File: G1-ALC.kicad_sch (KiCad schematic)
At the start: 90 parts, among them J101 Conn_01x03_Pin, J102 330 VAC In, J103 G1 connections, J104 105VAC in, J105 Conn_01x03_Pin, J107 Conn_01x05_Pin, J108 G2 Control board interconnect, Q101 TIP122, U101 LM7812_TO220, U102 LM324, U103 CNY17-4, U301 CNY17-4

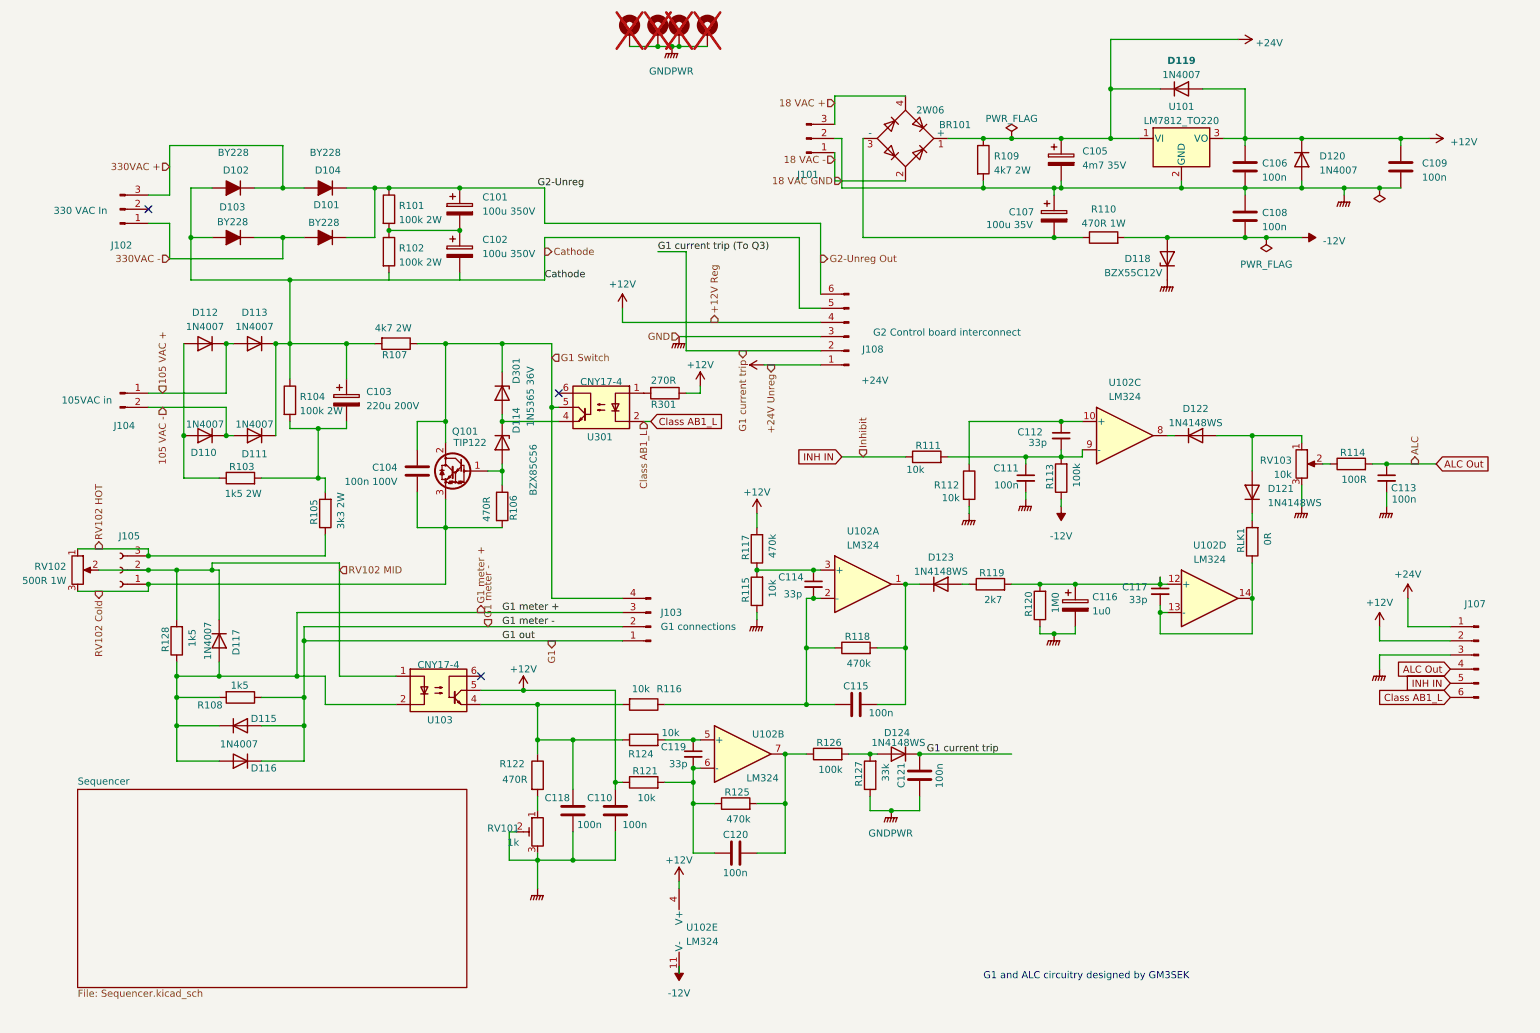
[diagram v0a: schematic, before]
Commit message: Fixes for issuees #1, €2 and #3
Fixed unconnected capacitor and bleeder
Turned connectors around to orient screw connectors with screws outward from the board.
Use new footprint for BY228 diodes with larget pand and holes.

Added a subsheet for notes containing differences with original drawing from GM3SEK.
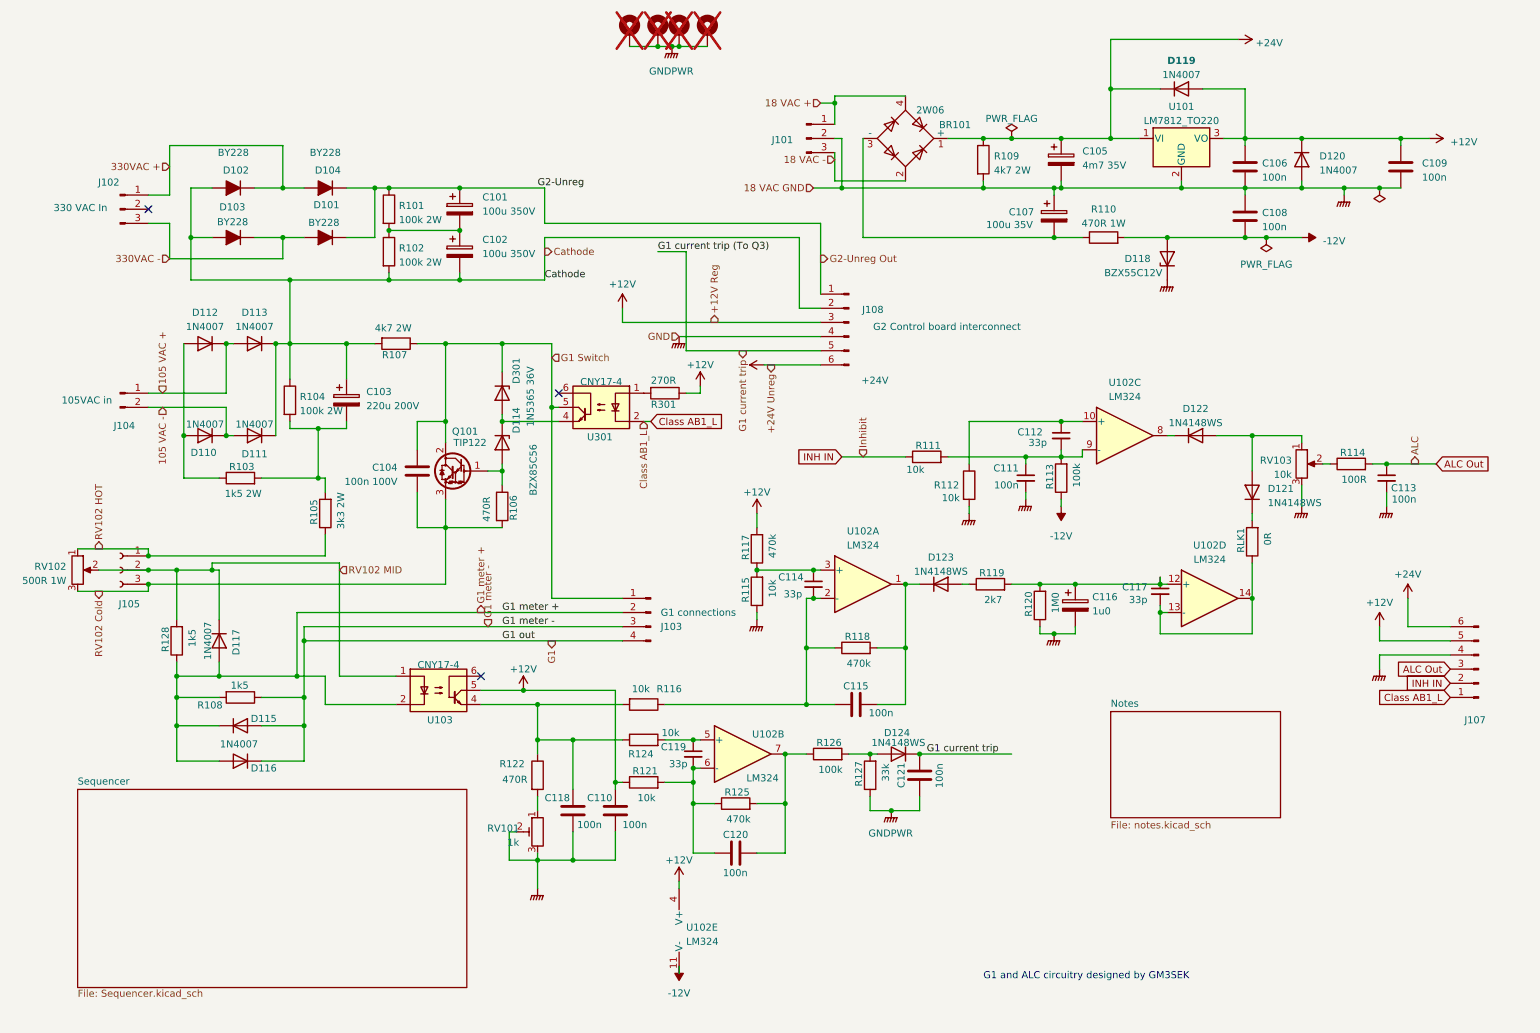
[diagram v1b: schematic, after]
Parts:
- D101, D102, D103, D104: footprint Diode_THT:D_DO-15_P15.24mm_Horizontal -> Diode_THT_AKL:D_SOD-64_P15.24mm_big_holes_Horizontal
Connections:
- net +12V: now also J107.5 (Pin_5), J108.3 (Pin_3); no longer J107.2 (Pin_2), J108.4 (Pin_4)
- net +24V: now also J107.6 (Pin_6), J108.6 (Pin_6); no longer J107.1 (Pin_1), J108.1 (Pin_1)
- net 18 VAC +: now also J101.1 (Pin_1); no longer J101.3 (Pin_3)
- net 330VAC +: now also J102.1 (Pin_1); no longer J102.3 (Pin_3)
- net 330VAC -: now also J102.3 (Pin_3); no longer J102.1 (Pin_1)
- net ALC Out: now also J107.3 (Pin_3); no longer J107.4 (Pin_4)
- net Cathode: now also C102.2, J108.2 (Pin_2), R102.2; no longer J108.5 (Pin_5)
- net Class AB1_L: now also J107.1 (Pin_1); no longer J107.6 (Pin_6)
- net G1: now also J103.3 (Pin_3), J103.4 (Pin_4); no longer J103.1 (Pin_1), J103.2 (Pin_2)
- net G1 Switch: now also J103.1 (Pin_1); no longer J103.4 (Pin_4)
- net G1 current trip: now also J108.5 (Pin_5); no longer J108.2 (Pin_2)
- net G1 meter +: now also J103.2 (Pin_2); no longer J103.3 (Pin_3)
- net G2-Unreg Out: now also J108.1 (Pin_1); no longer J108.6 (Pin_6)
- net GNDPWR: now also J107.4 (Pin_4), J108.4 (Pin_4); no longer BR101.2, J101.1 (Pin_1), J107.3 (Pin_3), J108.3 (Pin_3)
- net INH IN: now also J107.2 (Pin_2); no longer J107.5 (Pin_5)
- net RV102 Cold: now also J105.3 (Pin_3); no longer J105.1 (Pin_1)
- net RV102 HOT: now also J105.1 (Pin_1); no longer J105.3 (Pin_3)
- new net 18 VAC -: BR101.2, J101.3 (Pin_3)
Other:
- added sheet Notes (notes.kicad_sch)
- moved on the sheet: J103, J105, J107, J108

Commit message: Nil
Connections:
- net RV102 Cold: now also J105.1 (Pin_1); no longer J105.3 (Pin_3)
- net RV102 HOT: now also J105.3 (Pin_3); no longer J105.1 (Pin_1)
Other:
- moved on the sheet: J105
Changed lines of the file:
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@@
 	(symbol
 		(lib_id "Connector:Conn_01x03_Socket")
-		(at 33.02 116.84 0)
-		(mirror y)
+		(at 33.02 116.84 180)
 		(unit 1)
 		(exclude_from_sim no)
@@
 		(dnp no)
 		(property "Reference" "J105"
-			(at 34.671 122.936 0)
+			(at 34.671 110.744 0)
 			(effects
 				(font
@@
 		)
 		(property "Value" "Conn_01x03_Pin"
-			(at 33.655 121.412 0)
+			(at 33.655 112.268 0)
 			(effects
 				(font

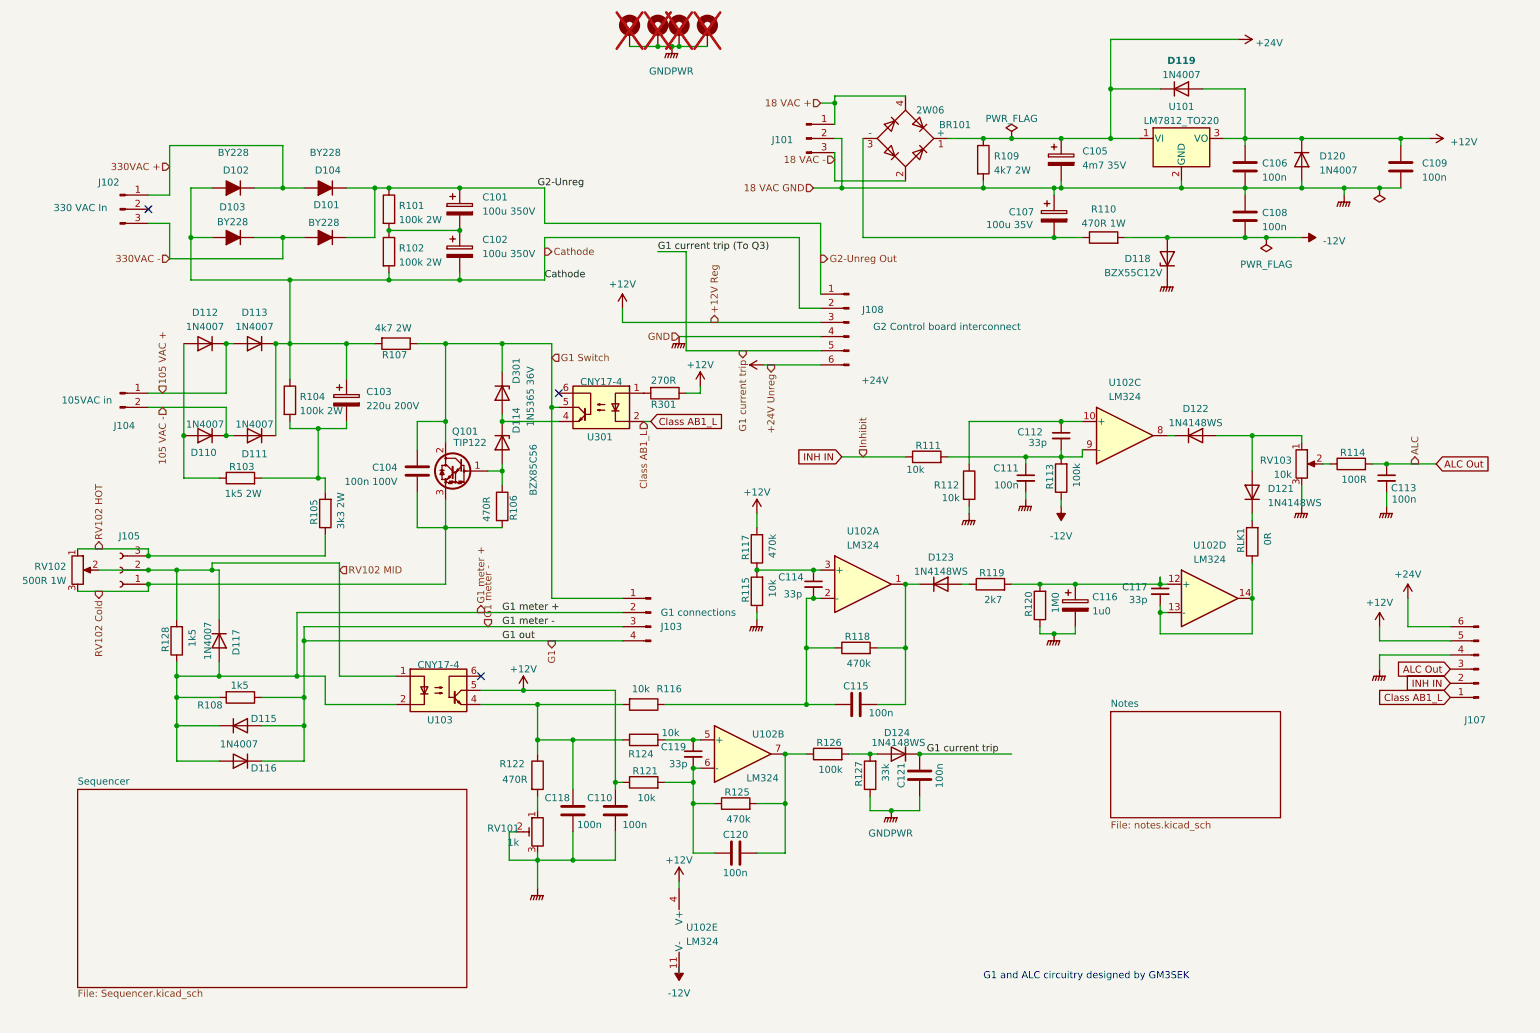
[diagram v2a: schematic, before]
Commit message: Updated junction positions and wire connections in schematic
Performed major modifications to the junction positions and wire connections in the kicad schematic G1-ALC. The changes include removal and addition of certain junction points, repositioning of wires and altering electrical connections to improve schematic efficiency and accuracy.
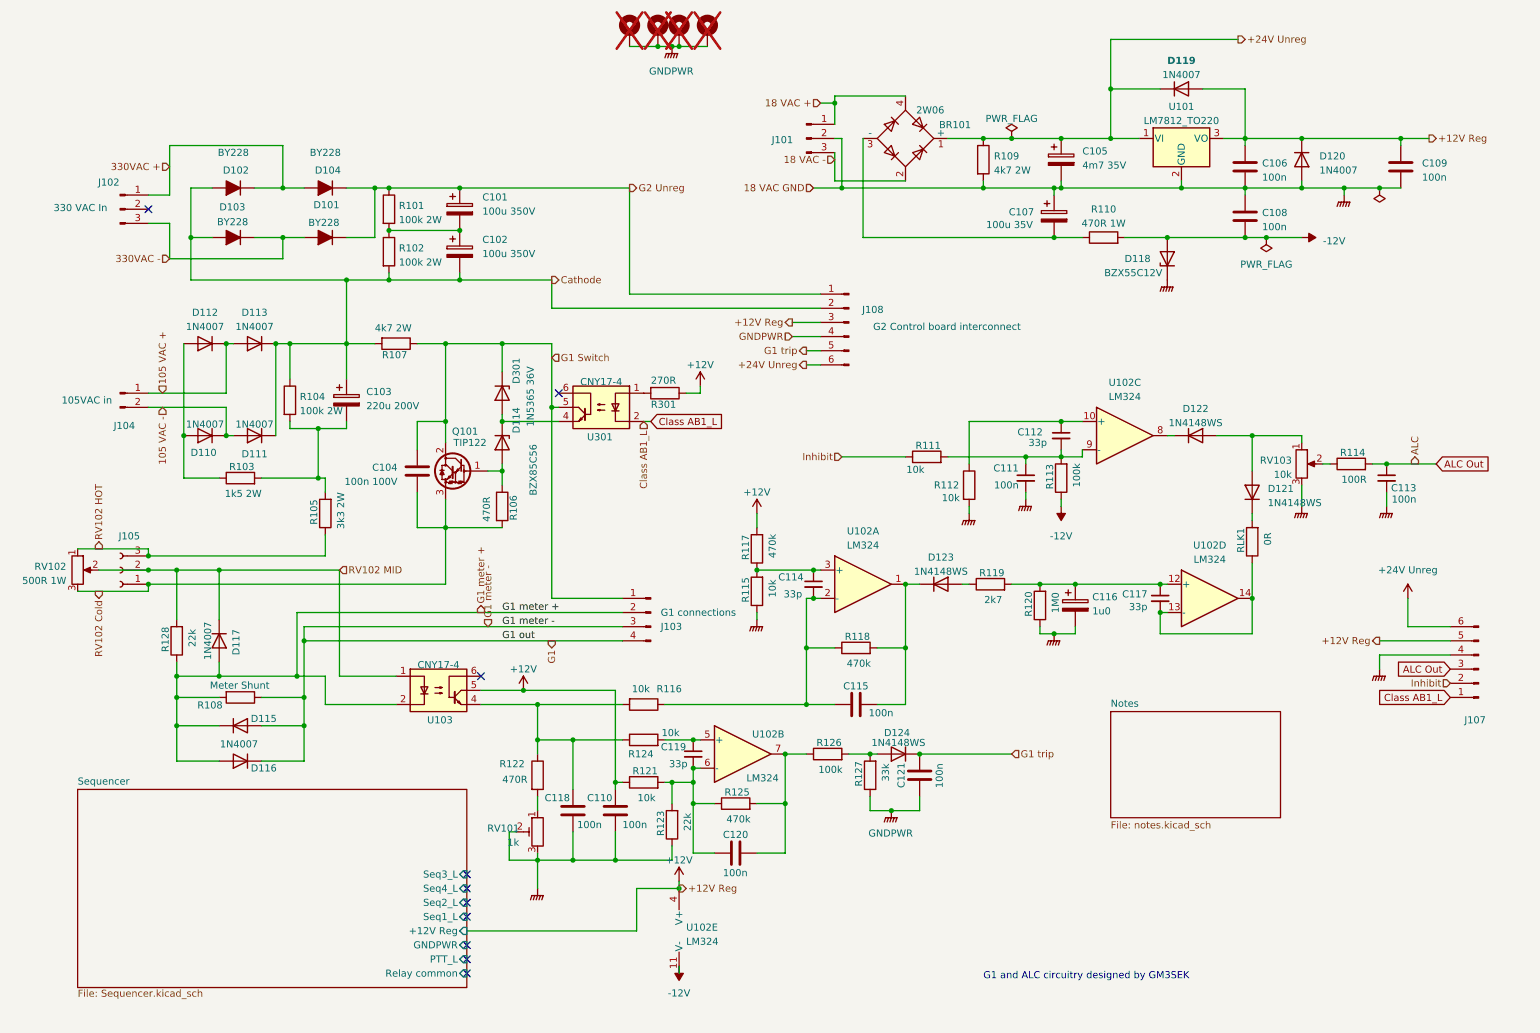
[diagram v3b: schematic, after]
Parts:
- added R123: 22k, Resistor_SMD:R_1206_3216Metric, symbol Device:R
- R108: value 1k5 -> Meter Shunt
- R128: value 1k5 -> 22k
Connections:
- net GNDPWR: now also R123.1
- net at C119.2, C120.1, R121.2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: now also R123.2
- net +24V renamed +24V Unreg
- net G1 current trip renamed G1 trip
- net G2-Unreg Out renamed G2 Unreg
- net INH IN renamed Inhibit
- no-connect marks 3 -> 10
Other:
- sheet Sequencer ports: added +12V Reg, GNDPWR, PTT_L, Relay common, Seq1_L, Seq2_L, Seq3_L, Seq4_L; removed none
- moved on the sheet: C117

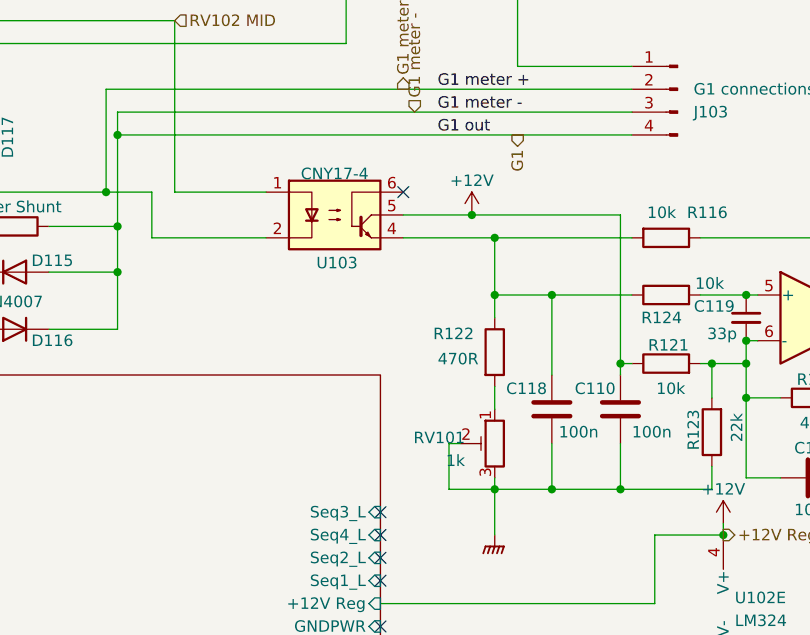
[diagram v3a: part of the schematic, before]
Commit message: Changed optocoupler U103 to a MCT5211
The optocoupler U103 must be as sensitive as the MCT5211. It could not be replaced by CNY17-4 despite what is said by Mouser when searching for the MCT5211. Fortunately DigiKey has a direct replacement with the same specifications: MCT5211M.
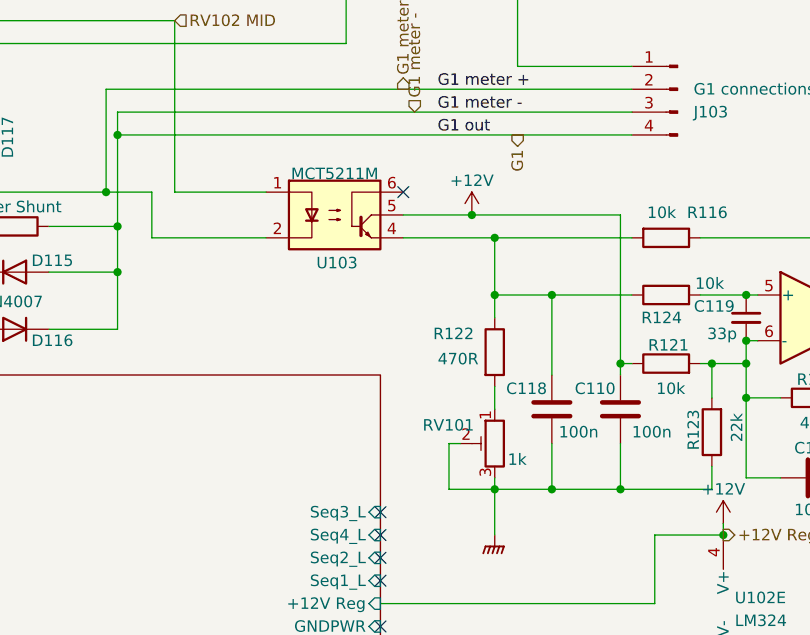
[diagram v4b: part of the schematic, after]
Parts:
- U103: value CNY17-4 -> MCT5211M; Notes (none) -> This component is crucial. It cannot simply be exchanged fo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; Order # 40301704 -> MCT5211M-ND; Supplier Electrokit -> DigiKey
- U301: Order # 40301704 -> 751-1268-5-ND; Supplier Electrokit -> DigiKey
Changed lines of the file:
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@@
 			)
 		)
-		(property "Value" "CNY17-4"
+		(property "Value" "MCT5211M"
 			(at 90.17 133.858 0)
 			(effects
@@
 			)
 		)
-		(property "Datasheet" "http://www.vishay.com/docs/83606/cny17.pdf"
+		(property "Datasheet" "https://www.onsemi.com/pdf/datasheet/mct5211m-d.pdf"
 			(at 90.17 138.43 0)
 			(effects
@@
 			)
 		)
-		(property "Description" ""
+		(property "Description" "Optoisolator Transistor with Base Output 4170Vrms 1 Channel 6-DIP CTR 110%@1mA"
 			(at 90.17 138.43 0)
 			(effects
@@
 			)
 		)
-		(property "Order #" "40301704"
+		(property "Order #" "MCT5211M-ND"
 			(at 90.17 138.43 0)
 			(effects
@@
 			)
 		)
-		(property "Supplier" "Electrokit"
+		(property "Supplier" "DigiKey"
 			(at 90.17 138.43 0)
 			(effects
@@
 			)
 		)
-		(property "Notes" ""
+		(property "Notes" "This component is crucial. It cannot simply be exchanged for any other optocoupler because its sensititity to low LED current is needed."
 			(at 90.17 138.43 0)
 			(effects
@@
 			)
 		)
-		(property "Datasheet" "http://www.vishay.com/docs/83606/cny17.pdf"
+		(property "Datasheet" "https://www.vishay.com/docs/83606/cny17.pdf"
 			(at 119.38 87.63 0)
 			(effects
@@
 			)
 		)
-		(property "Description" ""
+		(property "Description" "Optoisolator Transistor with Base Output "
 			(at 119.38 87.63 0)
 			(effects
@@
 			)
 		)
-		(property "Order #" "40301704"
+		(property "Order #" "751-1268-5-ND"
 			(at 119.38 87.63 0)
 			(effects
@@
 			)
 		)
-		(property "Supplier" "Electrokit"
+		(property "Supplier" "DigiKey"
 			(at 119.38 87.63 0)
 			(effects
@@
 		(dnp no)
 		(property "Reference" "RV101"
-			(at 104.648 163.195 0)
+			(at 105.664 161.798 0)
 			(effects
 				(font
@@
 		)
 		(property "Value" "1k"
-			(at 104.648 165.735 0)
+			(at 111.506 165.608 0)
 			(effects
 				(font
